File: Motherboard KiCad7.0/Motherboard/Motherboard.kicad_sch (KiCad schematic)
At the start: 92 parts, among them J1 USB_B_Micro, J10 430450200, J11 430450200, J12 430450200, J2 SWD_01x04_Pin, J3 430450200, J4 430450200, J5 B04B-XASK-1, J6 430450200, J7 430450200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

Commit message: Minor fixes
Added rev. number, list of contributors to layout. Added part numbers to some components in schematic. Generated BOMs using Kennan's plugin
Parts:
- J5: Digikey (none) -> 455-B04B-XASK-1-ND
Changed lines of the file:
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@@
       (effects (font (size 1.27 1.27) italic) hide)
+    )
+    (property "Digikey" "455-B04B-XASK-1-ND" (at 267.97 175.26 0)
+      (effects (font (size 1.27 1.27)) hide)
     )
     (pin "2")

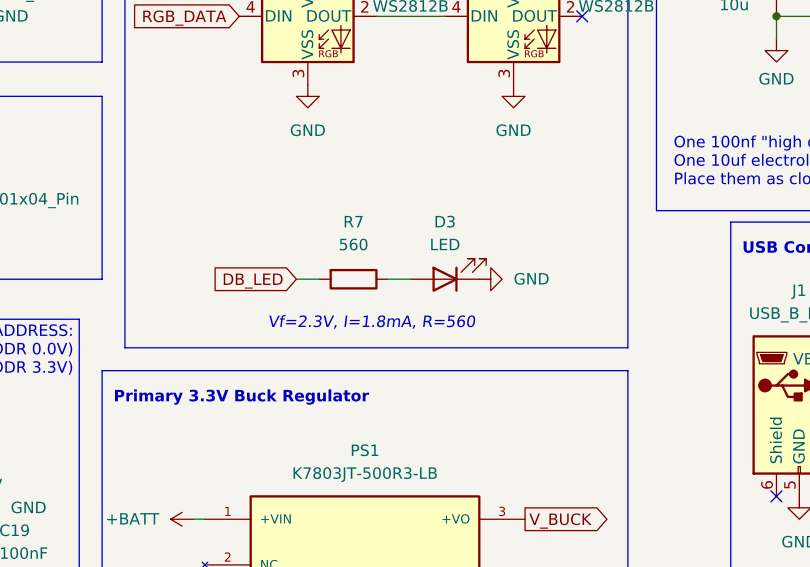
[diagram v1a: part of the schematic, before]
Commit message: Updated led resistor values
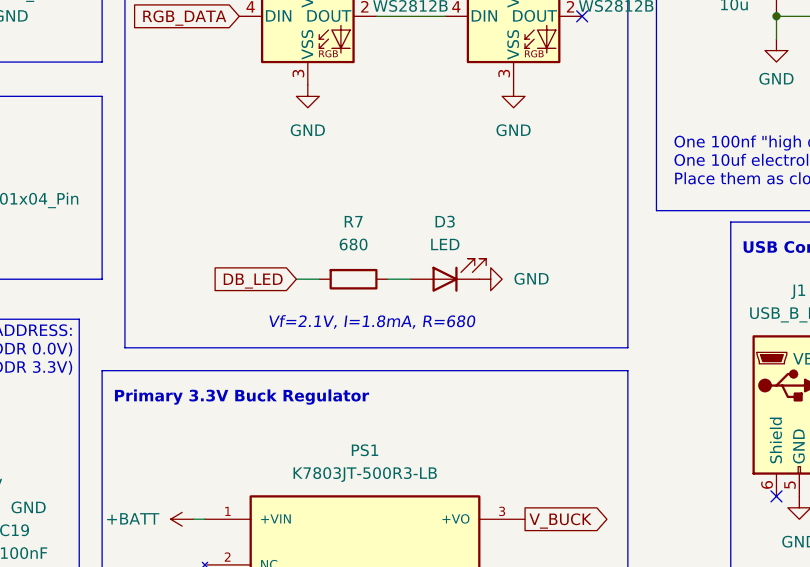
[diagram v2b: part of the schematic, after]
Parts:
- R7: value 560 -> 680; LCSC C23204 -> C23228
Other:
- note added: "Vf=2.1V, I=1.8mA, R=680"
- note removed: "Vf=2.3V, I=1.8mA, R=560"
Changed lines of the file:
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@@
     (effects (font (size 1.27 1.27)) (justify left bottom))
   )
-  (text "Vf=2.3V, I=1.8mA, R=560" (at 168.275 74.295 0)
+  (text "Vf=2.1V, I=1.8mA, R=680" (at 168.275 74.295 0)
     (effects (font (size 1.27 1.27) italic) (justify left bottom))
   )
@@
       (effects (font (size 1.27 1.27)))
     )
-    (property "Value" "560" (at 177.8 64.77 90)
+    (property "Value" "680" (at 177.8 64.77 90)
       (effects (font (size 1.27 1.27)))
     )
@@
       (effects (font (size 1.27 1.27)) hide)
     )
-    (property "LCSC" "C23204" (at 177.8 68.58 90)
-      (effects (font (size 1.27 1.27)) hide)
-    )
+    (property "LCSC" "C23228" (at 177.8 68.58 90)
+      (effects (font (size 1.27 1.27)) hide)
+    )

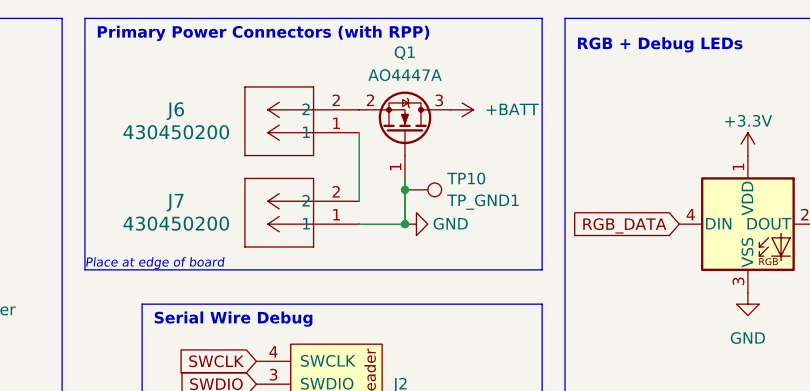
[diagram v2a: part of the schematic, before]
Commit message: Fixed AO444&A footprint
Fixed AO444&A footprint and symbol
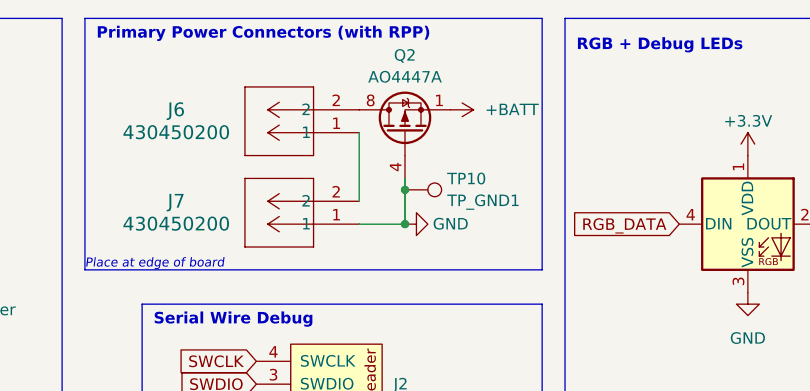
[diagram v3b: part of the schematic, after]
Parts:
- removed Q1: AO4447A, Package_TO_SOT_SMD:SOT-23, symbol Transistor_FET:AO3400A
- added Q2: AO4447A, Package_SO:SOIC-8_3.9x4.9mm_P1.27mm, symbol Transistor_FET:IRF7404
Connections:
- net +BATT: now also Q2.1 (S), Q2.2 (S), Q2.3 (S)
- net GND: now also Q2.4 (G)
- net at J6.2: now also Q2.5 (D), Q2.6 (D), Q2.7 (D), Q2.8 (D)
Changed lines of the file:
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@@
-    )
-  )
-  (symbol (lib_id "Transistor_FET:AO3400A") (at 134.62 29.21 270) (mirror x) (unit 1)
-    (in_bom yes) (on_board yes) (dnp no) (fields_autoplaced)
-    (property "Reference" "Q1" (at 134.62 20.32 90)
-      (effects (font (size 1.27 1.27)))
-    )
-    (property "Value" "AO4447A" (at 134.62 22.86 90)
-      (effects (font (size 1.27 1.27)))
-    )
-    (property "Footprint" "Package_TO_SOT_SMD:SOT-23" (at 132.715 24.13 0)
-      (effects (font (size 1.27 1.27) italic) (justify left) hide)
-    )
-    (property "Datasheet" "http://www.aosmd.com/pdfs/datasheet/AO3400A.pdf" (at 130.81 24.13 0)
-      (effects (font (size 1.27 1.27)) (justify left) hide)
-    )
-    (property "LCSC" "C125867" (at 134.62 29.21 90)
-      (effects (font (size 1.27 1.27)) hide)
-    )
-    (pin "1")
-    (pin "2")
-    (pin "3")
-    (instances
-      (project "Motherboard"
-        (path "/6c6aab7b-9fc7-4161-8073-41667e18c629"
-          (reference "Q1") (unit 1)
-        )
-      )
     )
   )
@@
         )
       )
+    )
+  )
+  (symbol (lib_id "Transistor_FET:IRF7404") (at 134.62 29.21 90) (unit 1)
+    (in_bom yes) (on_board yes) (dnp no) (fields_autoplaced)
+    (property "Reference" "Q2" (at 134.62 20.6207 90)
+      (effects (font (size 1.27 1.27)))
+    )
+    (property "Value" "AO4447A" (at 134.62 23.0449 90)
+      (effects (font (size 1.27 1.27)))
+    )
+    (property "Footprint" "Package_SO:SOIC-8_3.9x4.9mm_P1.27mm" (at 136.525 24.13 0)
+      (effects (font (size 1.27 1.27) italic) (justify left) hide)
+    )
+    (property "Datasheet" "https://datasheet.lcsc.com/lcsc/1806020932_Alpha---Omega-Semicon-AO4447A_C125867.pdf" (at 134.62 29.21 90)
+      (effects (font (size 1.27 1.27)) (justify left) hide)
+    )
+    (property "LCSC" "C125867" (at 134.62 29.21 90)
+      (effects (font (size 1.27 1.27)) hide)
+    )
+    (pin "1")
+    (pin "2")
+    (pin "3")
+    (pin "4")
+    (pin "5")
+    (pin "6")
+    (pin "7")
+    (pin "8")
+    (instances
+      (project "Motherboard"
+        (path "/6c6aab7b-9fc7-4161-8073-41667e18c629"
+          (reference "Q2") (unit 1)
+        )
+      )
